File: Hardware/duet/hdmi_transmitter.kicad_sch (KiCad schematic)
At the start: 1 part, among them U4 SII9022ACNU

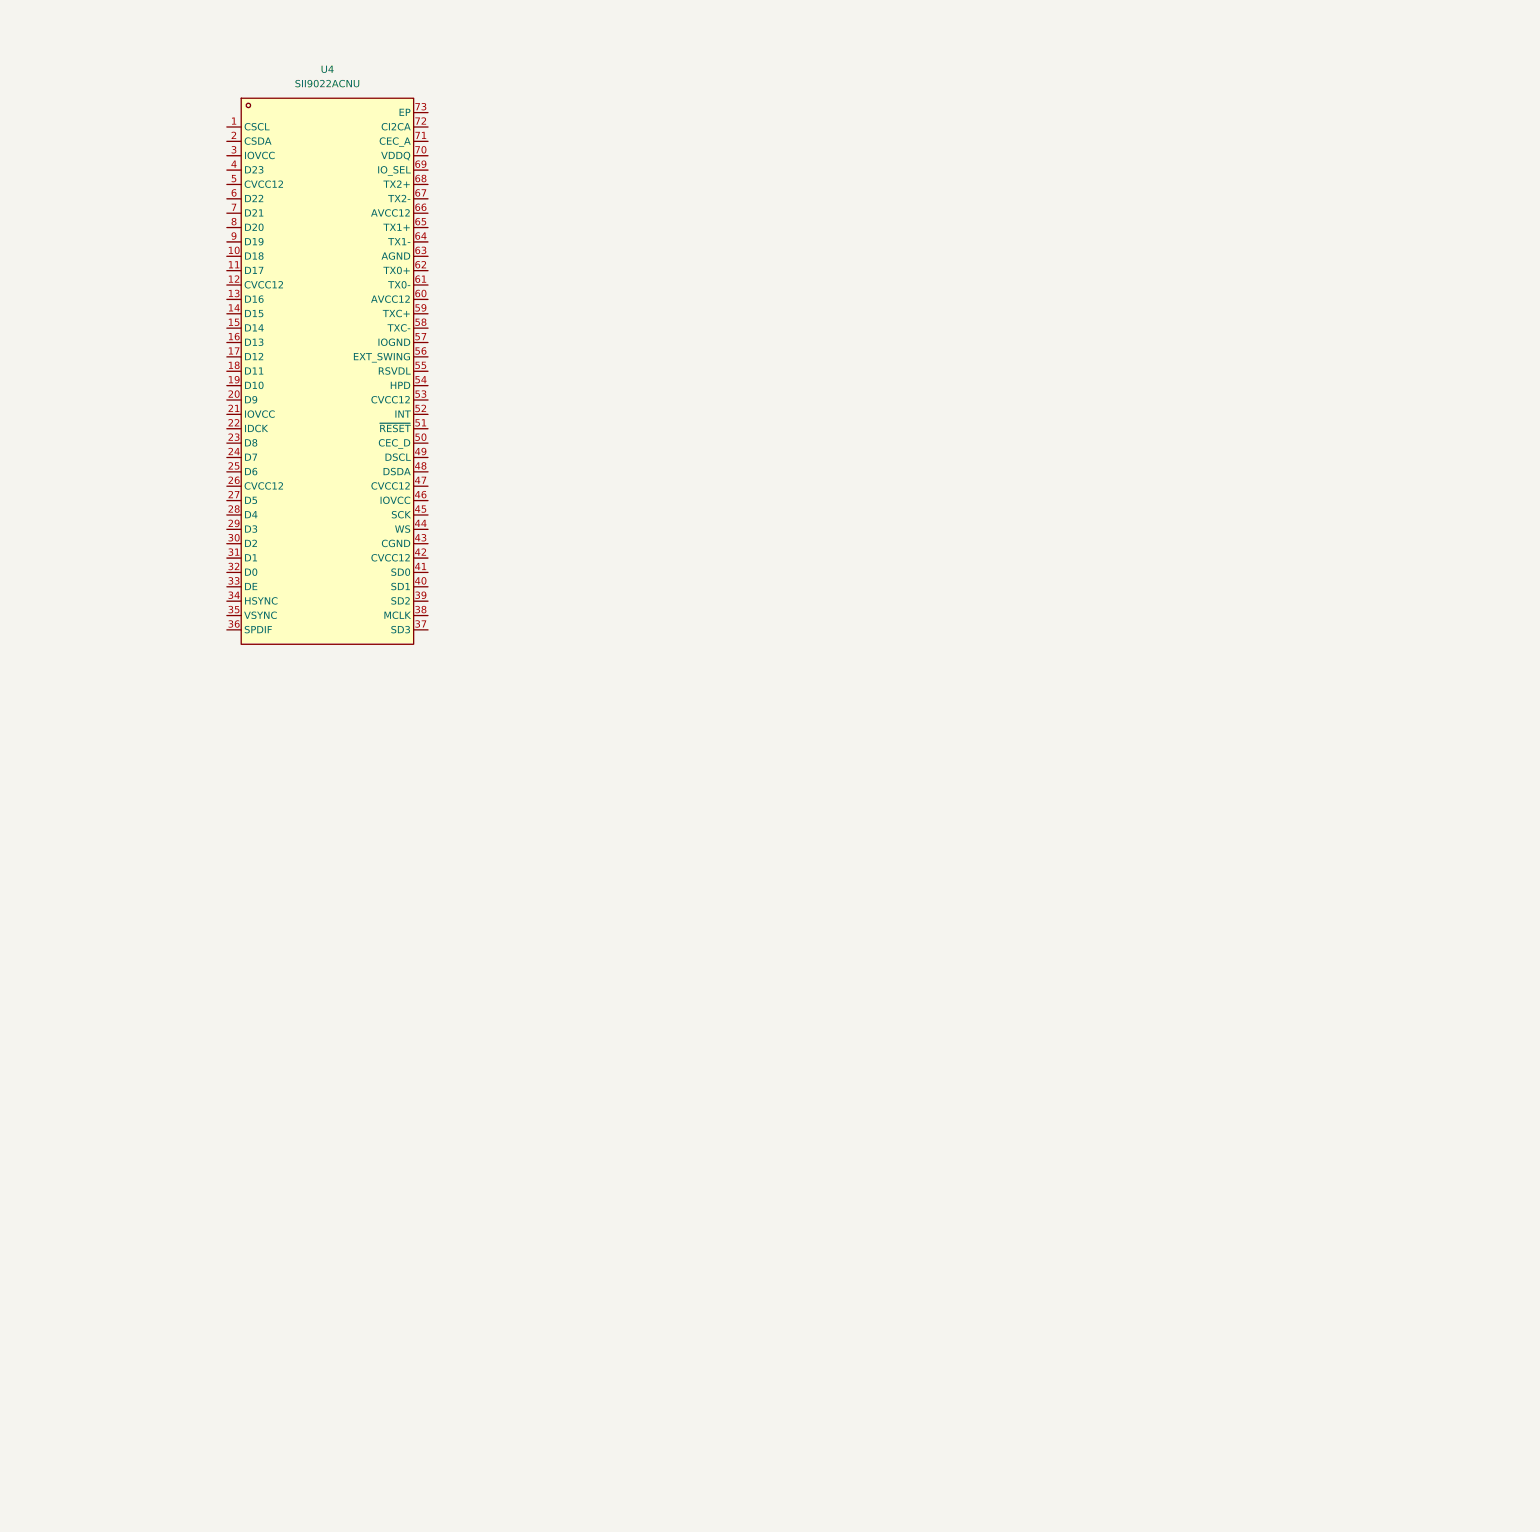
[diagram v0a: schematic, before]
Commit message: Adds HDMI transmitter and connector
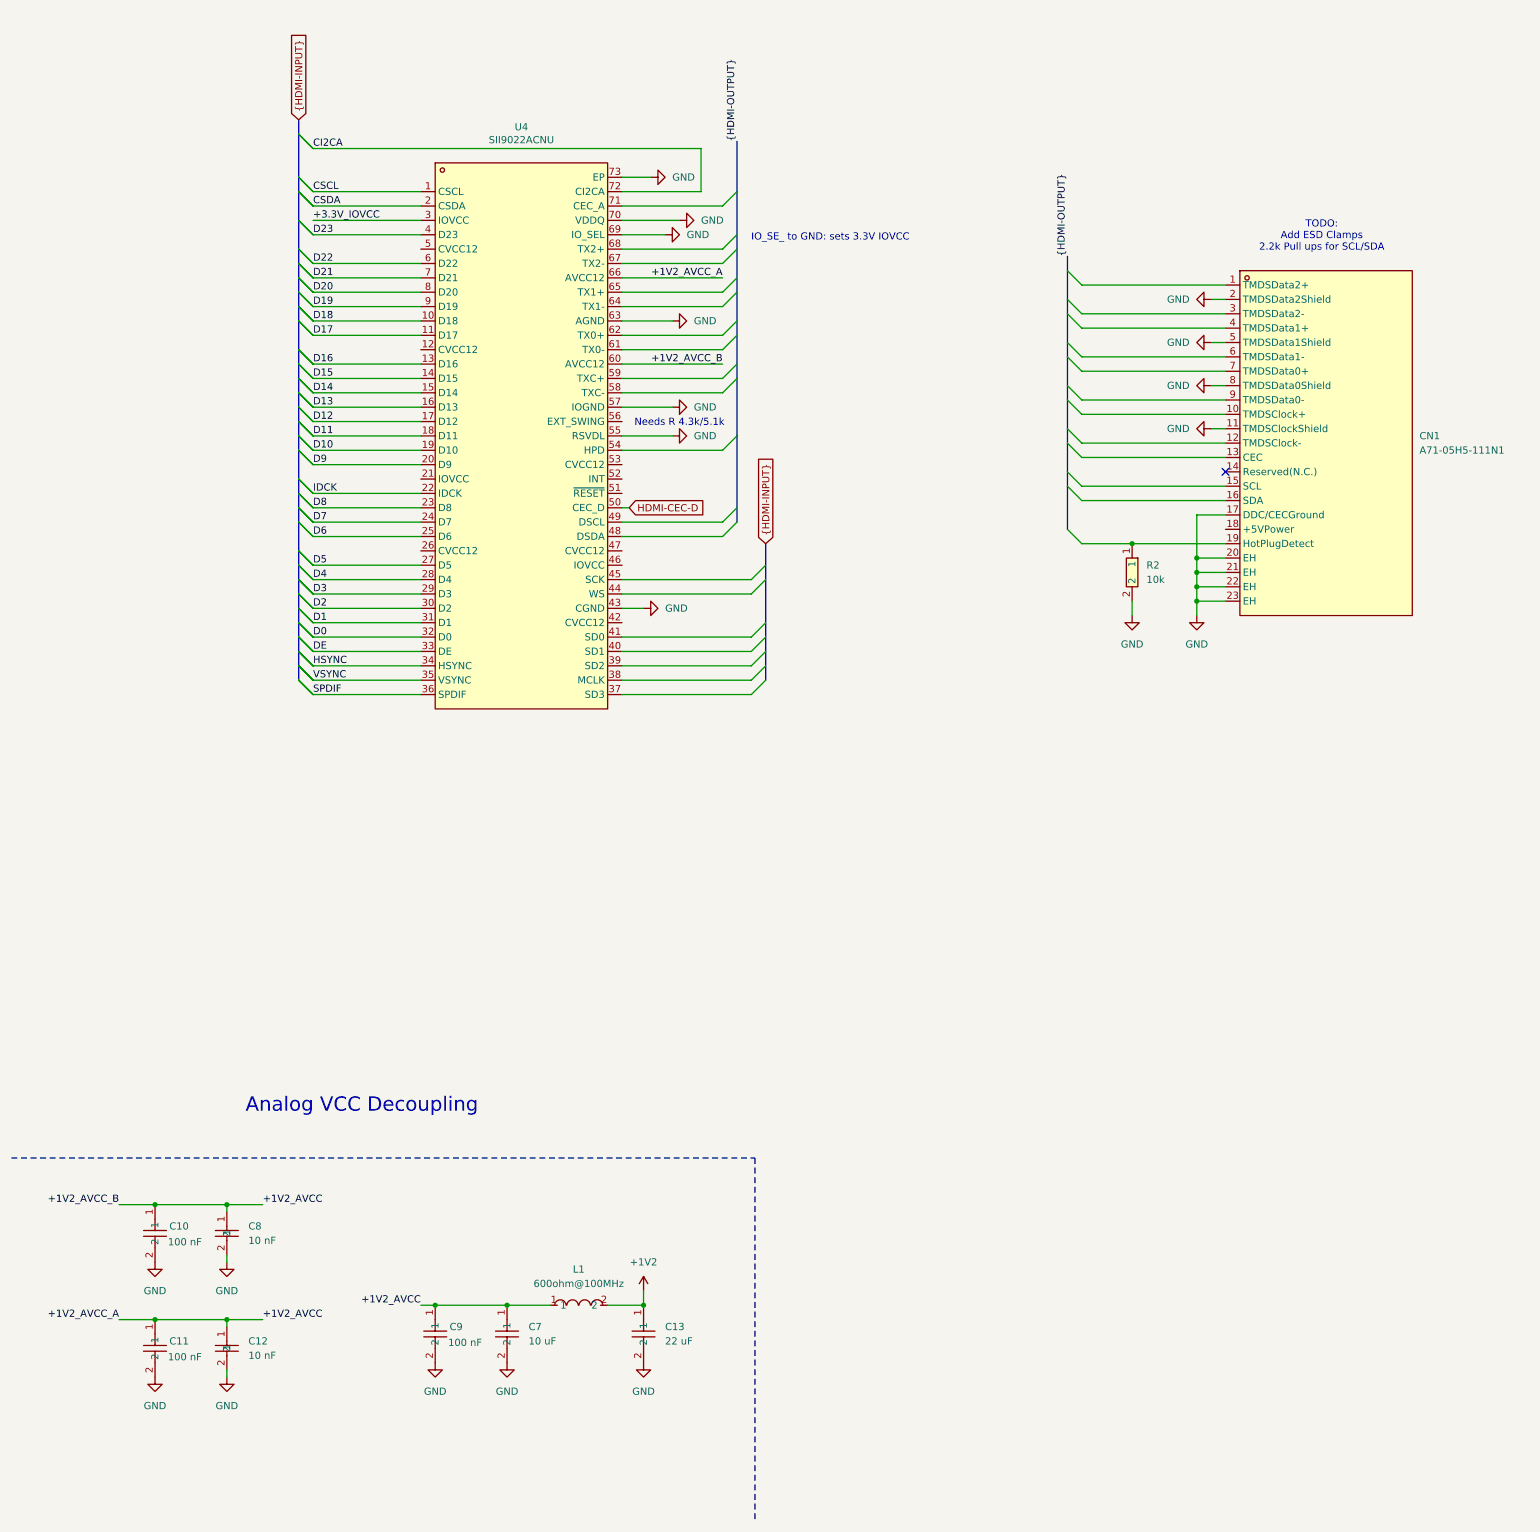
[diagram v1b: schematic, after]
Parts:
- added C10, C11, C9: 100 nF, easyeda2kicad:C0402, symbol easyeda2kicad:CL05B104KO5NNNC
- added C12, C8: 10 nF, easyeda2kicad:C0402, symbol easyeda2kicad:CL05B103KB5NNNC
- added C13: 22 uF, easyeda2kicad:C0805, symbol easyeda2kicad:CL21A226MAQNNNE
- added C7: 10 uF, easyeda2kicad:C0603, symbol easyeda2kicad:CL10A106MA8NRNC
- added CN1: A71-05H5-111N1, easyeda2kicad:HDMI-SMD_A71-05H5-111N1, symbol easyeda2kicad:A71-05H5-111N1
- added L1: 600ohm@100MHz, easyeda2kicad:L0603, symbol easyeda2kicad:GZ1608D601TF
- added R2: 10k, easyeda2kicad:R0402, symbol easyeda2kicad:0402WGF1002TCE
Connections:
- net CSCL: now reaches U4.1 (CSCL)
- net D18: now reaches U4.10 (D18)
- net D17: now reaches U4.11 (D17)
- net D16: now reaches U4.13 (D16)
- net D15: now reaches U4.14 (D15)
- net D14: now reaches U4.15 (D14)
- net D13: now reaches U4.16 (D13)
- net D12: now reaches U4.17 (D12)
- net D11: now reaches U4.18 (D11)
- net D10: now reaches U4.19 (D10)
- net CSDA: now reaches U4.2 (CSDA)
- net D9: now reaches U4.20 (D9)
- net IDCK: now reaches U4.22 (IDCK)
- net D8: now reaches U4.23 (D8)
- net D7: now reaches U4.24 (D7)
- net D6: now reaches U4.25 (D6)
- net D5: now reaches U4.27 (D5)
- net D4: now reaches U4.28 (D4)
- net D3: now reaches U4.29 (D3)
- net +3.3V_IOVCC: now reaches U4.3 (IOVCC)
- net D2: now reaches U4.30 (D2)
- net D1: now reaches U4.31 (D1)
- net D0: now reaches U4.32 (D0)
- net DE: now reaches U4.33 (DE)
- net HSYNC: now reaches U4.34 (HSYNC)
- net VSYNC: now reaches U4.35 (VSYNC)
- net SPDIF: now reaches U4.36 (SPDIF)
- net D23: now reaches U4.4 (D23)
- net GND: now reaches U4.43 (CGND)
- net GND: now also U4.55 (RSVDL), U4.57 (IOGND), U4.63 (AGND), U4.69 (IO_SEL), U4.70 (VDDQ), U4.73 (EP), C10.2, C11.2, C12.2, C13.2, C7.2, C8.2, C9.2, CN1.11 (TMDSClockShield), CN1.17 (DDC/CECGround), CN1.2 (TMDSData2Shield), CN1.20 (EH), CN1.21 (EH), CN1.22 (EH), CN1.23 (EH), CN1.5 (TMDSData1Shield), CN1.8 (TMDSData0Shield), R2.2
- net HDMI-CEC-D: now reaches U4.50 (CEC_D)
- net D22: now reaches U4.6 (D22)
- net +1V2_AVCC: now reaches U4.60 (AVCC12)
- net +1V2_AVCC: now also U4.66 (AVCC12), C10.1, C11.1, C12.1, C7.1, C8.1, C9.1, L1.1
- net D21: now reaches U4.7 (D21)
- net CI2CA: now reaches U4.72 (CI2CA)
- net D20: now reaches U4.8 (D20)
- net D19: now reaches U4.9 (D19)
- new net: CN1.19 (HotPlugDetect), R2.1
- new net +1V2: C13.1, L1.2
- no-connect marks 0 -> 1
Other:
- note added: "Analog VCC Decoupling"
- note added: "IO_SE_ to GND: sets 3.3V IOVCC"
- note added: "Needs R 4.3k/5.1k"
- note added: "TODO: Add ESD Clamps 2.2k Pull ups for SCL/SDA"
- moved on the sheet: U4

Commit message: Adds ESP32 and pull up-down resistors
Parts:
- added C14, C15, C16, C17, C18, C19, C21, C22, C23, C25, C26, C27: 100 nF, easyeda2kicad:C0402, symbol easyeda2kicad:CL05B104KO5NNNC
- added C20, C24: 10 uF, easyeda2kicad:C0603, symbol easyeda2kicad:CL10A106MA8NRNC
- added L2, L3: 600ohm@100MHz, easyeda2kicad:L0603, symbol easyeda2kicad:GZ1608D601TF
- added R10, R5, R6: 4.7k, easyeda2kicad:R0402, symbol easyeda2kicad:0402WGF4701TCE
- added R3, R4: 2.2k, easyeda2kicad:R0402, symbol easyeda2kicad:0402WGF2201TCE
- added R7: 100 Ohm, easyeda2kicad:R0402, symbol easyeda2kicad:0402WGF1000TCE
- added R8: 4.3k, easyeda2kicad:R0402, symbol easyeda2kicad:0402WGF4301TCE
- added U7, U8: RCLAMP0514M, easyeda2kicad:MSOP-10_L3.0-W3.0-P0.50-LS5.0-BL, symbol easyeda2kicad:RCLAMP0514M
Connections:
- net +1V2: now also C20.1, L2.2
- net +3.3V_IOVCC: now also U4.21 (IOVCC), U4.46 (IOVCC), C21.1, C22.1, C23.1, L3.1
- net CI2CA: now also R10.1
- net CSCL: now also R5.1
- net CSDA: now also R6.1
- net GND: now also C14.2, C15.2, C16.2, C17.2, C18.2, C19.2, C20.2, C21.2, C22.2, C23.2, C24.2, C25.2, C26.2, C27.2, R8.2, U7.8 (GND), U8.8 (GND)
- net +1V2_CVCC: now reaches U4.12 (CVCC12)
- net +1V2_CVCC: now also U4.26 (CVCC12), U4.42 (CVCC12), U4.47 (CVCC12), U4.5 (CVCC12), U4.53 (CVCC12), C14.1, C15.1, C16.1, C17.1, C18.1, C19.1, L2.1
- net DSDA: now reaches U4.48 (DSDA)
- net DSDA: now also CN1.16 (SDA), R4.1
- net DSCL: now reaches U4.49 (DSCL)
- net DSCL: now also CN1.15 (SCL), R3.1
- net HDMI-RESET: now reaches U4.51 (~{RESET})
- net HDMI-INT: now reaches U4.52 (INT)
- net HPD: now reaches U4.54 (HPD)
- net HPD: now also CN1.19 (HotPlugDetect), R2.1
- net EXT_SWING: now reaches U4.56 (EXT_SWING)
- net EXT_SWING: now also R8.1
- net TXC-: now reaches U4.58 (TXC-)
- net TXC-: now also CN1.12 (TMDSClock-), U7.6 (LINE4)
- net TXC+: now reaches U4.59 (TXC+)
- net TXC+: now also CN1.10 (TMDSClock+), U7.9 (LINE2)
- net TX0-: now reaches U4.61 (TX0-)
- net TX0-: now also CN1.9 (TMDSData0-), U7.4 (LINE3)
- net TX0+: now reaches U4.62 (TX0+)
- net TX0+: now also CN1.7 (TMDSData0+), U7.1 (LINE1)
- net TX1-: now reaches U4.64 (TX1-)
- net TX1-: now also CN1.6 (TMDSData1-), U8.6 (LINE4)
- net TX1+: now reaches U4.65 (TX1+)
- net TX1+: now also CN1.4 (TMDSData1+), U8.9 (LINE2)
- net TX2-: now reaches U4.67 (TX2-)
- net TX2-: now also CN1.3 (TMDSData2-), U8.4 (LINE3)
- net TX2+: now reaches U4.68 (TX2+)
- net TX2+: now also CN1.1 (TMDSData2+), U8.1 (LINE1)
- net CEC_A: now reaches U4.71 (CEC_A)
- net CEC_A: now also CN1.13 (CEC)
- net +5V_HDMI: now reaches CN1.18 (+5VPower)
- net +5V_HDMI: now also C25.1, R7.2
- new net +3.3V: C24.1, C26.1, C27.1, R10.2, R5.2, R6.2, U7.3 (VCC), U8.3 (VCC)
- new net +5V: R3.2, R4.2, R7.1
- no-connect marks 1 -> 9
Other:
- note added: "Core VCC Decoupling"
- note added: "HDMI Connector"
- note added: "HDMI Connector ESD Protection"
- note added: "HDMI Transmitter"
- note added: "IO VCC Decoupling"
- note added: "Pull up/down resistors"
- note removed: "Needs R 4.3k/5.1k"
- note removed: "TODO: Add ESD Clamps 2.2k Pull ups for SCL/SDA"
- moved on the sheet: CN1, R2, U4

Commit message: Add mezzanine connector and finalze HDMI
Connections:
- net SD3: now reaches U4.37 (SD3)
- net MCLK: now reaches U4.38 (MCLK)
- net SD2: now reaches U4.39 (SD2)
- net SD1: now reaches U4.40 (SD1)
- net SD0: now reaches U4.41 (SD0)
- net WS: now reaches U4.44 (WS)
- net SCK: now reaches U4.45 (SCK)
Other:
- note added: "IO_SEL to GND: sets 3.3V IOVCC"
- note removed: "IO_SE_ to GND: sets 3.3V IOVCC"
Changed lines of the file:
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@@
 		)
 	)
-	(text "IO_SE_ to GND: sets 3.3V IOVCC"
+	(text "IO_SEL to GND: sets 3.3V IOVCC"
 		(exclude_from_sim no)
 		(at 206.756 77.978 0)
@@
 	)
 	(bus_entry
-		(at 110.49 62.23)
-		(size -2.54 -2.54)
-		(stroke
-			(width 0)
-			(type default)
-		)
-	)
-	(bus_entry
 		(at 186.69 128.27)
 		(size 2.54 -2.54)
@@
 	)
 	(bus_entry
-		(at 110.49 69.85)
-		(size -2.54 -2.54)
-		(stroke
-			(width 0)
-			(type default)
-		)
-	)
-	(bus_entry
 		(at 317.5 96.52)
 		(size 2.54 2.54)
@@
 	)
 	(bus_entry
-		(at 107.95 69.85)
-		(size 2.54 2.54)
-		(stroke
-			(width 0)
-			(type default)
-		)
-	)
-	(bus_entry
 		(at 317.5 106.68)
 		(size 2.54 2.54)
@@
 	)
 	(bus_entry
-		(at 110.49 72.39)
-		(size -2.54 -2.54)
-		(stroke
-			(width 0)
-			(type default)
-		)
-	)
-	(bus_entry
 		(at 107.95 125.73)
 		(size 2.54 2.54)
@@
 	)
 	(bus_entry
-		(at 107.95 67.31)
-		(size 2.54 2.54)
-		(stroke
-			(width 0)
-			(type default)
-		)
-	)
-	(bus_entry
 		(at 107.95 102.87)
 		(size 2.54 2.54)
@@
 	)
 	(bus_entry
-		(at 107.95 59.69)
-		(size 2.54 2.54)
-		(stroke
-			(width 0)
-			(type default)
-		)
-	)
-	(bus_entry
 		(at 107.95 153.67)
 		(size 2.54 2.54)
@@
 	(wire
 		(pts
-			(xy 165.1 74.93) (xy 175.26 74.93)
+			(xy 165.1 74.93) (xy 173.99 74.93)
 		)
 		(stroke
@@
 	(wire
 		(pts
-			(xy 165.1 69.85) (xy 179.07 69.85)
+			(xy 165.1 69.85) (xy 184.15 69.85)
 		)
 		(stroke
@@
 	(wire
 		(pts
-			(xy 110.49 69.85) (xy 129.54 69.85)
-		)
-		(stroke
-			(width 0)
-			(type default)
-		)
-	)
-	(wire
-		(pts
 			(xy 165.1 87.63) (xy 186.69 87.63)
 		)
@@
 	(wire
 		(pts
-			(xy 110.49 72.39) (xy 129.54 72.39)
+			(xy 123.19 72.39) (xy 129.54 72.39)
 		)
 		(stroke
@@
 	(wire
 		(pts
-			(xy 71.12 203.2) (xy 71.12 207.01)
+			(xy 123.19 69.85) (xy 129.54 69.85)
 		)
 		(stroke
@@
 	(wire
 		(pts
-			(xy 215.9 260.35) (xy 215.9 261.62)
+			(xy 71.12 203.2) (xy 71.12 207.01)
 		)
 		(stroke
@@
 	(wire
 		(pts
-			(xy 71.12 207.01) (xy 78.74 207.01)
+			(xy 215.9 260.35) (xy 215.9 261.62)
 		)
 		(stroke
@@
 	(wire
 		(pts
-			(xy 104.14 207.01) (xy 113.03 207.01)
+			(xy 71.12 207.01) (xy 78.74 207.01)
 		)
 		(stroke
@@
 	(wire
 		(pts
-			(xy 179.07 69.85) (xy 179.07 62.23)
+			(xy 104.14 207.01) (xy 113.03 207.01)
 		)
 		(stroke
@@
 	(wire
 		(pts
-			(xy 110.49 62.23) (xy 179.07 62.23)
-		)
-		(stroke
-			(width 0)
-			(type default)
-		)
-	)
-	(wire
-		(pts
 			(xy 165.1 125.73) (xy 171.45 125.73)
 		)
@@
 	(wire
 		(pts
-			(xy 110.49 74.93) (xy 129.54 74.93)
+			(xy 114.3 74.93) (xy 129.54 74.93)
 		)
 		(stroke
@@
 		)
 	)
+	(label "SD1"
+		(at 166.37 151.13 0)
+		(effects
+			(font
+				(size 1.27 1.27)
+			)
+			(justify left bottom)
+		)
+	)
 	(label "TX0-"
 		(at 186.69 97.79 180)
@@
 		)
 	)
-	(label "CI2CA"
-		(at 110.49 62.23 0)
+	(label "SD3"
+		(at 166.37 158.75 0)
 		(effects
 			(font
@@
 		)
 	)
+	(label "CI2CA"
+		(at 184.15 69.85 180)
+		(effects
+			(font
+				(size 1.27 1.27)
+			)
+			(justify right bottom)
+		)
+	)
 	(label "D5"
 		(at 110.49 135.89 0)
@@
 	)
 	(label "+3.3V_IO_A"
-		(at 110.49 74.93 0)
+		(at 114.3 74.93 0)
 		(effects
 			(font
@@
 		)
 	)
+	(label "SD0"
+		(at 166.37 148.59 0)
+		(effects
+			(font
+				(size 1.27 1.27)
+			)
+			(justify left bottom)
+		)
+	)
 	(label "{HDMI-OUTPUT}"
 		(at 189.23 60.96 90)
@@
 		)
 	)
+	(label "WS"
+		(at 166.37 140.97 0)
+		(effects
+			(font
+				(size 1.27 1.27)
+			)
+			(justify left bottom)
+		)
+	)
 	(label "CSCL"
 		(at 233.68 224.79 180)
@@
 		)
 	)
+	(label "SD2"
+		(at 166.37 153.67 0)
+		(effects
+			(font
+				(size 1.27 1.27)
+			)
+			(justify left bottom)
+		)
+	)
 	(label "D1"
 		(at 110.49 146.05 0)
@@
 	)
 	(label "CSDA"
-		(at 110.49 72.39 0)
+		(at 123.19 72.39 0)
 		(effects
 			(font
@@
 	)
 	(label "CSCL"
-		(at 110.49 69.85 0)
+		(at 123.19 69.85 0)
 		(effects
 			(font
@@
 		)
 	)
+	(label "MCLK"
+		(at 166.37 156.21 0)
+		(effects
+			(font
+				(size 1.27 1.27)
+			)
+			(justify left bottom)
+		)
+	)
 	(label "HPD"
 		(at 186.69 115.57 180)
@@
 		)
 	)
+	(label "SCK"
+		(at 166.37 138.43 0)
+		(effects
+			(font
+				(size 1.27 1.27)
+			)
+			(justify left bottom)
+		)
+	)
 	(label "CEC_A"
 		(at 320.04 109.22 0)
@@
 	(symbol
 		(lib_id "power:GND")
-		(at 175.26 74.93 90)
+		(at 173.99 74.93 90)
 		(unit 1)
 		(body_style 1)
@@
 		(fields_autoplaced yes)
 		(property "Reference" "#PWR017"
-			(at 181.61 74.93 0)
+			(at 180.34 74.93 0)
 			(hide yes)
 			(show_name no)
@@
 		)
 		(property "Value" "GND"
-			(at 179.07 74.9299 90)
+			(at 177.8 74.9299 90)
 			(show_name no)
 			(do_not_autoplace no)
@@
 		)
 		(property "Footprint" ""
-			(at 175.26 74.93 0)
+			(at 173.99 74.93 0)
 			(hide yes)
 			(show_name no)
@@
 		)
 		(property "Datasheet" ""
-			(at 175.26 74.93 0)
+			(at 173.99 74.93 0)
 			(hide yes)
 			(show_name no)
@@
 		)
 		(property "Description" "Power symbol creates a global label with name \"GND\" , ground"
-			(at 175.26 74.93 0)
+			(at 173.99 74.93 0)
 			(hide yes)
 			(show_name no)
